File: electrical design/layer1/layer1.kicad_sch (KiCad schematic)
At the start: 95 parts, among them J1 Conn_01x08_Male, J2 Conn_01x06_Female, SW1 SW_DPDT_x2, SW2 SW_DPDT_x2, SW3 SW_Push, U1 STM32F103C8T6, U2 CD74HC4067SM, U3 CD74HC4067SM, Y1 8MHz

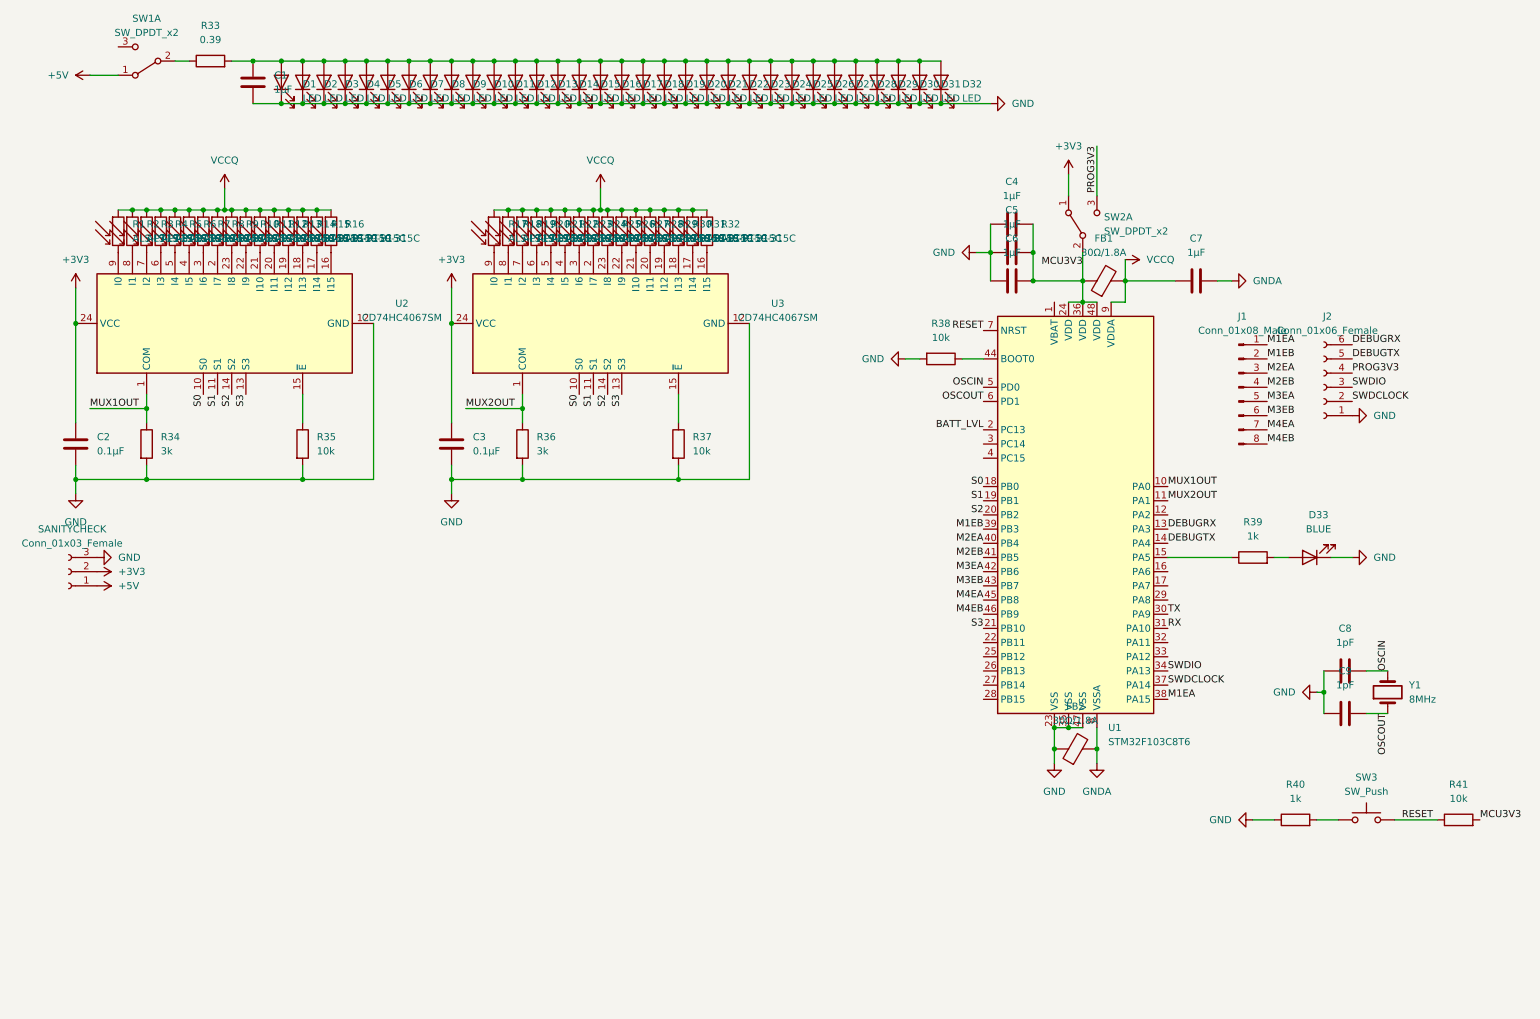
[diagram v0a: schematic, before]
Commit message: add solenoid circuit and custom board rules
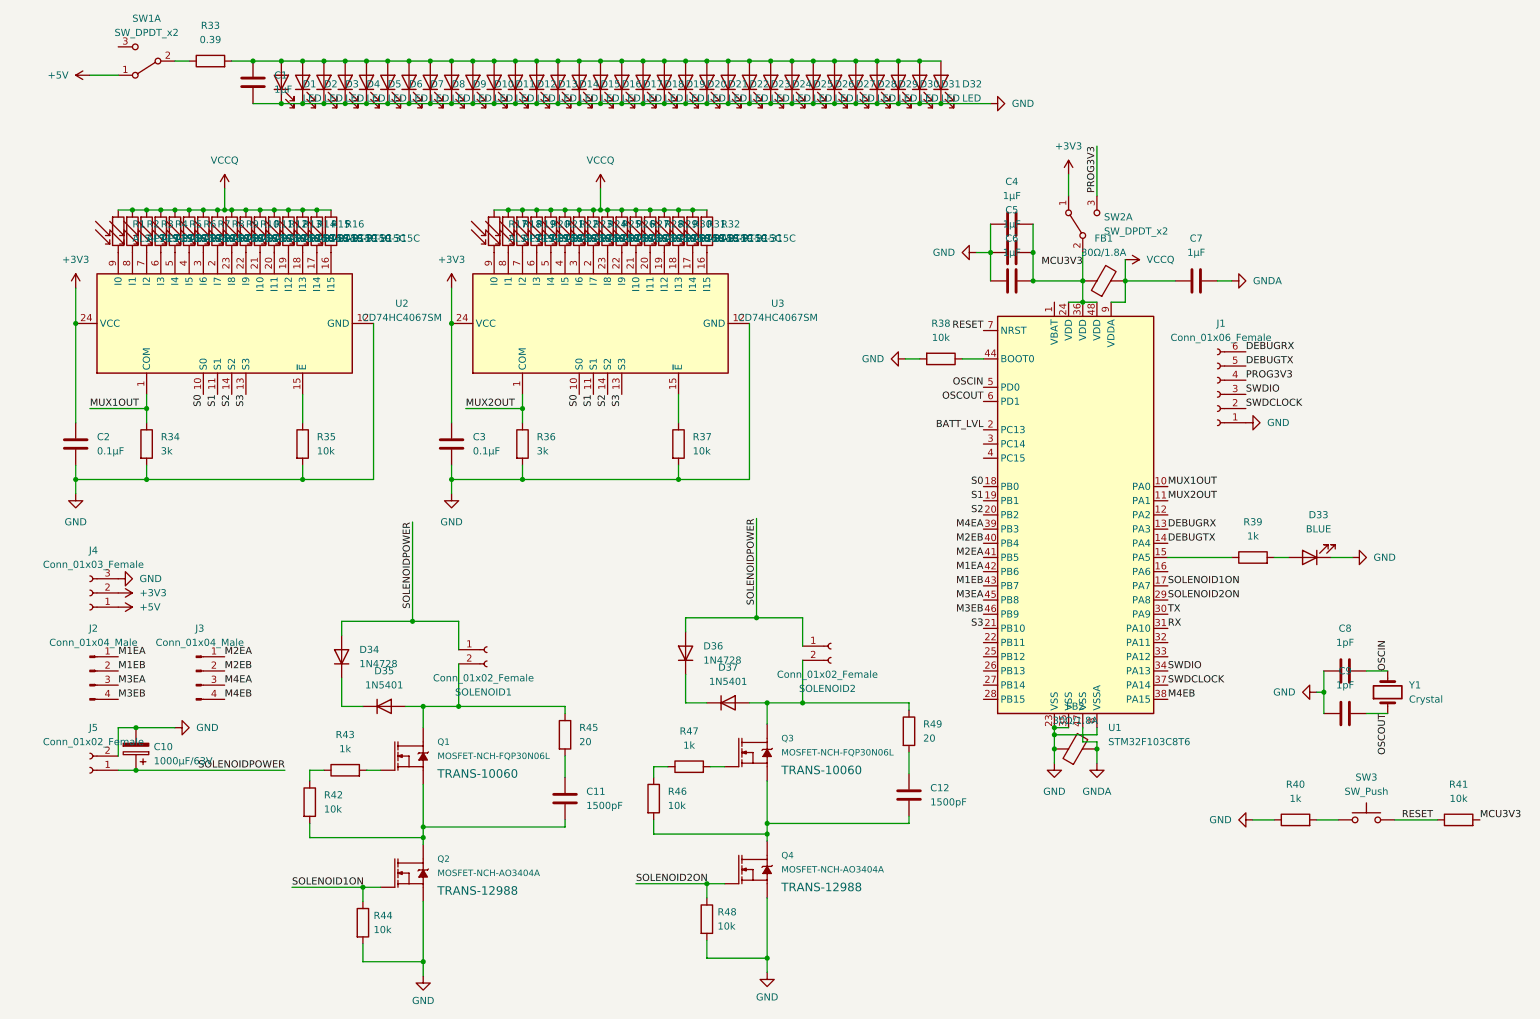
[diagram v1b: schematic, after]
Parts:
- removed J1: Conn_01x08_Male, symbol Connector:Conn_01x08_Male
- added C10: 1000µF/63V, Capacitor_THT:CP_Radial_D16.0mm_P7.50mm, symbol Device:C_Polarized
- added C11, C12: 1500pF, Capacitor_SMD:C_0603_1608Metric, symbol Device:C
- added D34, D36: 1N4728, Diode_THT:D_DO-41_SOD81_P10.16mm_Horizontal, symbol Device:D
- added D35, D37: 1N5401, Diode_THT:D_DO-27_P15.24mm_Horizontal, symbol Device:D
- added J2, J3: Conn_01x04_Male, Connector_PinHeader_2.54mm:PinHeader_1x04_P2.54mm_Vertical, symbol Connector:Conn_01x04_Male
- added J5, SOLENOID1, SOLENOID2: Conn_01x02_Female, Connector_AMASS:AMASS_XT30UPB-F_1x02_P5.0mm_Vertical, symbol Connector:Conn_01x02_Female
- added Q1, Q3: MOSFET-NCH-FQP30N06L, Package_TO_SOT_THT:TO-220-3_Vertical, symbol SparkFun-DiscreteSemi:MOSFET-NCH-FQP30N06L
- added Q2, Q4: MOSFET-NCH-AO3404A, Package_TO_SOT_SMD:TSOT-23, symbol SparkFun-DiscreteSemi:MOSFET-NCH-AO3404A
- added R42, R44, R46, R48: 10k, Resistor_SMD:R_0603_1608Metric, symbol Device:R
- added R43, R47: 1k, Resistor_SMD:R_0603_1608Metric, symbol Device:R
- added R45, R49: 20, Resistor_SMD:R_0603_1608Metric, symbol Device:R
- C2, C3, C4, C5, C6, C7, FB1, FB2: footprint (none) -> Capacitor_SMD:C_0603_1608Metric
- C8, C9: footprint Capacitors:0603 -> Capacitor_SMD:C_0603_1608Metric
- D33: footprint (none) -> Diode_SMD:D_0603_1608Metric
- J4: renamed from SANITYCHECK; footprint (none) -> Connector_PinHeader_2.54mm:PinHeader_1x03_P2.54mm_Vertical
- R1, R10, R11, R12, R13, R14, R15, R16, R17, R18, R19, R2, R20, R21, R22, R23, R24, R25, R26, R27, R28, R29, R3, R30, R31, R32, R4, R5, R6, R7, R8, R9: footprint Diode_SMD:D_0201_0603Metric -> Resistor_SMD:R_0603_1608Metric
- R33, R34, R35, R36, R37, R38, R39, R40, R41: footprint (none) -> Resistor_SMD:R_0603_1608Metric
- SW3: footprint (none) -> Button_Switch_SMD:SW_Push_SPST_NO_Alps_SKRK
- Y1: value 8MHz -> Crystal
- renumbered J2 to J1
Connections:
- net GND: now also U1.8 (VSSA), C10.2, J5.2 (Pin_2), Q2.2 (S), Q4.2 (S), R44.2, R48.2; no longer U1.47 (VSS)
- net GNDA: now also U1.47 (VSS); no longer U1.8 (VSSA)
- net M1EA: now also U1.42 (PB6), J2.1 (Pin_1); no longer U1.38 (PA15)
- net M1EB: now also U1.43 (PB7), J2.2 (Pin_2); no longer U1.39 (PB3)
- net M2EA: now also U1.41 (PB5), J3.1 (Pin_1); no longer U1.40 (PB4)
- net M2EB: now also U1.40 (PB4), J3.2 (Pin_2); no longer U1.41 (PB5)
- net M3EA: now also U1.45 (PB8), J2.3 (Pin_3); no longer U1.42 (PB6)
- net M3EB: now also U1.46 (PB9), J2.4 (Pin_4); no longer U1.43 (PB7)
- net M4EA: now also U1.39 (PB3), J3.3 (Pin_3); no longer U1.45 (PB8)
- net M4EB: now also U1.38 (PA15), J3.4 (Pin_4); no longer U1.46 (PB9)
- net SOLENOID1ON: now reaches U1.17 (PA7)
- net SOLENOID1ON: now also Q2.1 (G), R44.1
- net SOLENOID2ON: now reaches U1.29 (PA8)
- net SOLENOID2ON: now also Q4.1 (G), R48.1
- new net: R42.1, R43.1
- new net: Q1.1 (G), R43.2
- new net: Q3.1 (G), R47.2
- new net: D37.2 (A), Q3.2 (D), R49.1, SOLENOID2.2 (Pin_2)
- new net: C12.2, Q3.3 (S), Q4.3 (D), R46.2
- new net: C11.2, Q1.3 (S), Q2.3 (D), R42.2
- new net: D36.1 (K), D37.1 (K)
- new net: D35.2 (A), Q1.2 (D), R45.1, SOLENOID1.2 (Pin_2)
- new net: R46.1, R47.1
- new net: C12.1, R49.2
- new net: D34.1 (K), D35.1 (K)
- new net: C11.1, R45.2
- new net SOLENOIDPOWER: C10.1, D34.2 (A), D36.2 (A), J5.1 (Pin_1), SOLENOID1.1 (Pin_1), SOLENOID2.1 (Pin_1)
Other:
- moved on the sheet: J1, J4

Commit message: update layer 1 and layer 3 pcbs
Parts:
- removed C12: 1500pF, Capacitor_SMD:C_0603_1608Metric, symbol Device:C
- removed D36: 1N4728, Diode_THT:D_DO-41_SOD81_P10.16mm_Horizontal, symbol Device:D
- removed D37: 1N5401, Diode_THT:D_DO-27_P15.24mm_Horizontal, symbol Device:D
- removed J2, J3: Conn_01x04_Male, Connector_PinHeader_2.54mm:PinHeader_1x04_P2.54mm_Vertical, symbol Connector:Conn_01x04_Male
- removed Q3: MOSFET-NCH-FQP30N06L, Package_TO_SOT_THT:TO-220-3_Vertical, symbol SparkFun-DiscreteSemi:MOSFET-NCH-FQP30N06L
- removed Q4: MOSFET-NCH-AO3404A, Package_TO_SOT_SMD:TSOT-23, symbol SparkFun-DiscreteSemi:MOSFET-NCH-AO3404A
- removed R46, R48: 10k, Resistor_SMD:R_0603_1608Metric, symbol Device:R
- removed R47: 1k, Resistor_SMD:R_0603_1608Metric, symbol Device:R
- removed R49: 20, Resistor_SMD:R_0603_1608Metric, symbol Device:R
- removed SOLENOID2: Conn_01x02_Female, Connector_AMASS:AMASS_XT30UPB-F_1x02_P5.0mm_Vertical, symbol Connector:Conn_01x02_Female
- J1: value Conn_01x06_Female -> SH1.0 Female
- SW1, SW2: footprint (none) -> Switches:SWITCH_SPDT_PTH_11.6X4.0MM_LOCK
- Y1: footprint Clocks:CRYSTAL-SMD-5X3.2-2PAD -> Crystal:Crystal_SMD_5032-2Pin_5.0x3.2mm
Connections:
- net M1EA: no longer names the net of U1.42 (PB6)
- net M1EB: no longer names the net of U1.43 (PB7)
- net M2EA: no longer names the net of U1.41 (PB5)
- net M2EB: no longer names the net of U1.40 (PB4)
- net M3EA: no longer names the net of U1.45 (PB8)
- net M3EB: no longer names the net of U1.46 (PB9)
- net M4EA: no longer names the net of U1.39 (PB3)
- net M4EB: no longer names the net of U1.38 (PA15)
- net SOLENOID1ON renamed SOLENOIDON
- net SOLENOID2ON: no longer names the net of U1.29 (PA8)

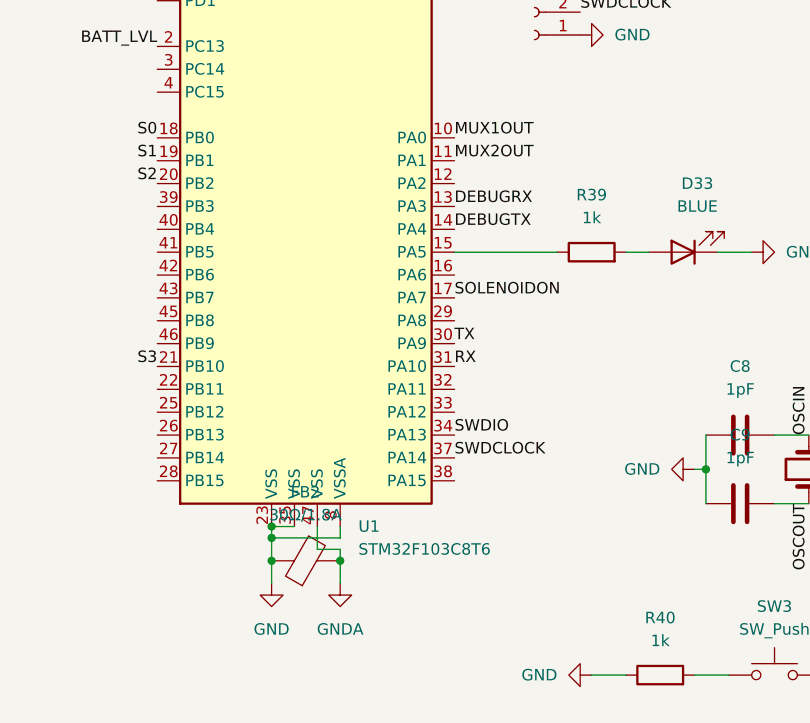
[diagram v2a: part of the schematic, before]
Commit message: update l1, l3, and driver pcbs
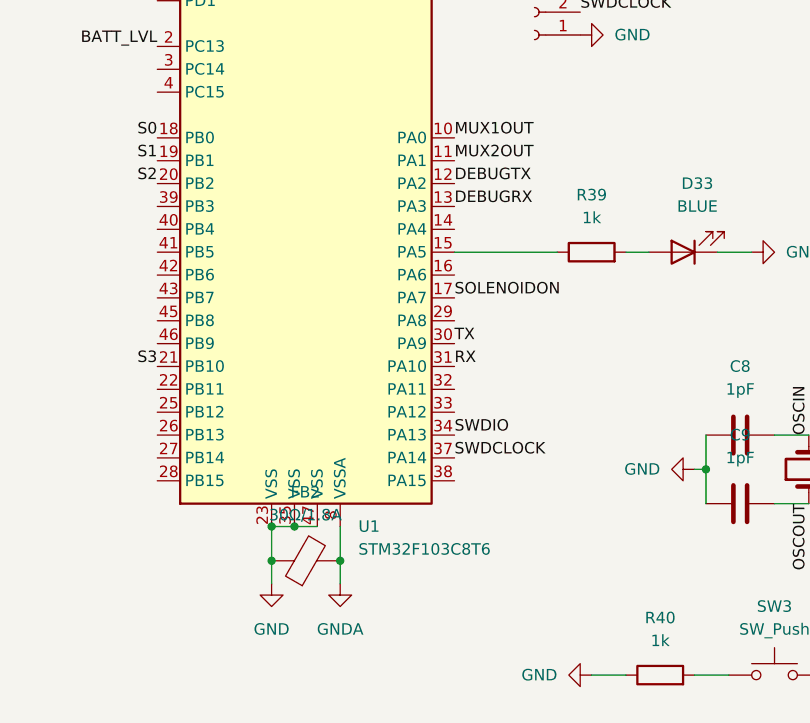
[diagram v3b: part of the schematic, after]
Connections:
- net DEBUGTX: now also U1.12 (PA2); no longer U1.14 (PA4)
- net GND: now also U1.47 (VSS); no longer U1.8 (VSSA)
- net GNDA: now also U1.8 (VSSA); no longer U1.47 (VSS)
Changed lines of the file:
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@@
   (junction (at 58.42 25.4) (diameter 0) (color 0 0 0 0)
   )
-  (junction (at 196.85 146.05) (diameter 0) (color 0 0 0 0)
-  )
   (junction (at 123.19 25.4) (diameter 0) (color 0 0 0 0)
   )
@@
   (junction (at 115.57 52.07) (diameter 0) (color 0 0 0 0)
   )
+  (junction (at 199.39 144.78) (diameter 0) (color 0 0 0 0)
+  )
   (junction (at 66.04 33.02) (diameter 0) (color 0 0 0 0)
   )
@@
     (stroke (width 0) (type default) (color 0 0 0 0))
   )
-  (wire (pts (xy 196.85 144.78) (xy 196.85 146.05))
-    (stroke (width 0) (type default) (color 0 0 0 0))
-  )
   (wire (pts (xy 52.07 52.07) (xy 54.61 52.07))
     (stroke (width 0) (type default) (color 0 0 0 0))
@@
     (stroke (width 0) (type default) (color 0 0 0 0))
   )
-  (wire (pts (xy 196.85 146.05) (xy 196.85 148.59))
+  (wire (pts (xy 196.85 144.78) (xy 196.85 148.59))
     (stroke (width 0) (type default) (color 0 0 0 0))
   )
@@
     (stroke (width 0) (type default) (color 0 0 0 0))
   )
-  (wire (pts (xy 204.47 147.32) (xy 204.47 148.59))
-    (stroke (width 0) (type default) (color 0 0 0 0))
-  )
   (wire (pts (xy 199.39 68.58) (xy 201.93 68.58))
     (stroke (width 0) (type default) (color 0 0 0 0))
@@
     (stroke (width 0) (type default) (color 0 0 0 0))
   )
-  (wire (pts (xy 204.47 144.78) (xy 204.47 146.05))
-    (stroke (width 0) (type default) (color 0 0 0 0))
-  )
   (wire (pts (xy 54.61 52.07) (xy 57.15 52.07))
     (stroke (width 0) (type default) (color 0 0 0 0))
@@
     (stroke (width 0) (type default) (color 0 0 0 0))
   )
-  (wire (pts (xy 201.93 144.78) (xy 201.93 147.32))
-    (stroke (width 0) (type default) (color 0 0 0 0))
-  )
   (wire (pts (xy 53.34 25.4) (xy 58.42 25.4))
     (stroke (width 0) (type default) (color 0 0 0 0))
@@
     (stroke (width 0) (type default) (color 0 0 0 0))
   )
+  (wire (pts (xy 204.47 144.78) (xy 204.47 148.59))
+    (stroke (width 0) (type default) (color 0 0 0 0))
+  )
   (wire (pts (xy 96.52 33.02) (xy 100.33 33.02))
     (stroke (width 0) (type default) (color 0 0 0 0))
@@
     (stroke (width 0) (type default) (color 0 0 0 0))
   )
-  (wire (pts (xy 201.93 147.32) (xy 204.47 147.32))
-    (stroke (width 0) (type default) (color 0 0 0 0))
-  )
   (wire (pts (xy 58.42 25.4) (xy 62.23 25.4))
     (stroke (width 0) (type default) (color 0 0 0 0))
@@
     (stroke (width 0) (type default) (color 0 0 0 0))
   )
+  (wire (pts (xy 199.39 144.78) (xy 201.93 144.78))
+    (stroke (width 0) (type default) (color 0 0 0 0))
+  )
   (wire (pts (xy 204.47 148.59) (xy 204.47 151.13))
     (stroke (width 0) (type default) (color 0 0 0 0))
@@
     (stroke (width 0) (type default) (color 0 0 0 0))
   )
-  (wire (pts (xy 204.47 146.05) (xy 196.85 146.05))
-    (stroke (width 0) (type default) (color 0 0 0 0))
-  )
   (wire (pts (xy 62.23 100.33) (xy 34.29 100.33))
     (stroke (width 0) (type default) (color 0 0 0 0))
@@
     (effects (font (size 1.27 1.27)) (justify right bottom))
   )
+  (label "DEBUGTX" (at 217.17 106.68 0)
+    (effects (font (size 1.27 1.27)) (justify left bottom))
+  )
   (label "PROG3V3" (at 204.47 40.64 270)
     (effects (font (size 1.27 1.27)) (justify right bottom))
@@
     (effects (font (size 1.27 1.27)) (justify right bottom))
   )
-  (label "DEBUGTX" (at 217.17 111.76 0)
-    (effects (font (size 1.27 1.27)) (justify left bottom))
-  )
   (label "OSCOUT" (at 184.15 86.36 180)

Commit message: almost final pcbs
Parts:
- added J2: SH1.0 5P, Connector_JST:JST_SH_BM05B-SRSS-TB_1x05-1MP_P1.00mm_Vertical, symbol Connector:Conn_01x05_Male
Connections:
- net +3V3: now also J2.4 (Pin_4)
- net +5V: now also J2.3 (Pin_3)
- net GND: now also J2.5 (Pin_5)
- net RX: now also J2.1 (Pin_1)
- net TX: now also J2.2 (Pin_2)
- net BATT_LVL: no longer names the net of U1.2 (PC13)
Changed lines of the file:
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@@
   (title_block
     (title "layer 1 schematic drawing")
-    (date "2023-01-10")
-    (rev "v0.4")
+    (date "2023-02-05")
+    (rev "v0.5")
     (company "8076 Robotics")
   )
@@
     (effects (font (size 1.27 1.27)) (justify right bottom))
   )
+  (label "RX" (at 146.05 173.99 0)
+    (effects (font (size 1.27 1.27)) (justify left bottom))
+  )
   (label "RX" (at 217.17 127 0)
     (effects (font (size 1.27 1.27)) (justify left bottom))
@@
     (effects (font (size 1.27 1.27)) (justify left bottom))
   )
+  (label "TX" (at 146.05 176.53 0)
+    (effects (font (size 1.27 1.27)) (justify left bottom))
+  )
   (label "S3" (at 119.38 85.09 270)
     (effects (font (size 1.27 1.27)) (justify right bottom))
@@
     (effects (font (size 1.27 1.27)) (justify left bottom))
   )
-  (label "BATT_LVL" (at 184.15 91.44 180)
-    (effects (font (size 1.27 1.27)) (justify right bottom))
-  )
   (label "S0" (at 44.45 85.09 270)
     (effects (font (size 1.27 1.27)) (justify right bottom))
@@
     (pin "2")
   )
+  (symbol (lib_id "power:+3V3") (at 146.05 181.61 270) (unit 1)
+    (in_bom yes) (on_board yes) (fields_autoplaced)
+    (property "Reference" "#PWR022" (id 0) (at 142.24 181.61 0)
+      (effects (font (size 1.27 1.27)) hide)
+    )
+    (property "Value" "+3V3" (id 1) (at 149.86 181.6099 90)
+      (effects (font (size 1.27 1.27)) (justify left))
+    )
+    (property "Footprint" "" (id 2) (at 146.05 181.61 0)
+      (effects (font (size 1.27 1.27)) hide)
+    )
+    (property "Datasheet" "" (id 3) (at 146.05 181.61 0)
+      (effects (font (size 1.27 1.27)) hide)
+    )
+    (pin "1")
+  )
   (symbol (lib_id "power:VCCQ") (at 209.55 60.96 270) (unit 1)
     (in_bom yes) (on_board yes) (fields_autoplaced)
@@
     (pin "2")
   )
+  (symbol (lib_id "Connector:Conn_01x05_Male") (at 140.97 179.07 0) (unit 1)
+    (in_bom yes) (on_board yes) (fields_autoplaced)
+    (property "Reference" "J2" (id 0) (at 141.605 168.91 0))
+    (property "Value" "SH1.0 5P" (id 1) (at 141.605 171.45 0))
+    (property "Footprint" "Connector_JST:JST_SH_BM05B-SRSS-TB_1x05-1MP_P1.00mm_Vertical" (id 2) (at 140.97 179.07 0)
+      (effects (font (size 1.27 1.27)) hide)
+    )
+    (property "Datasheet" "~" (id 3) (at 140.97 179.07 0)
+      (effects (font (size 1.27 1.27)) hide)
+    )
+    (pin "1")
+    (pin "2")
+    (pin "3")
+    (pin "4")
+    (pin "5")
+  )
   (symbol (lib_id "Connector:Conn_01x02_Female") (at 24.13 152.4 180) (unit 1)
     (in_bom yes) (on_board yes) (fields_autoplaced)
@@
     (pin "1")
   )
+  (symbol (lib_id "power:+5V") (at 146.05 179.07 270) (unit 1)
+    (in_bom yes) (on_board yes) (fields_autoplaced)
+    (property "Reference" "#PWR021" (id 0) (at 142.24 179.07 0)
+      (effects (font (size 1.27 1.27)) hide)
+    )
+    (property "Value" "+5V" (id 1) (at 149.86 179.0699 90)
+      (effects (font (size 1.27 1.27)) (justify left))
+    )
+    (property "Footprint" "" (id 2) (at 146.05 179.07 0)
+      (effects (font (size 1.27 1.27)) hide)
+    )
+    (property "Datasheet" "" (id 3) (at 146.05 179.07 0)
+      (effects (font (size 1.27 1.27)) hide)
+    )
+    (pin "1")
+  )
   (symbol (lib_id "Device:R") (at 101.6 93.98 0) (unit 1)
     (in_bom yes) (on_board yes) (fields_autoplaced)
@@
     (pin "2")
   )
+  (symbol (lib_id "power:GND") (at 146.05 184.15 90) (unit 1)
+    (in_bom yes) (on_board yes) (fields_autoplaced)
+    (property "Reference" "#PWR023" (id 0) (at 152.4 184.15 0)
+      (effects (font (size 1.27 1.27)) hide)
+    )
+    (property "Value" "GND" (id 1) (at 149.86 184.1499 90)
+      (effects (font (size 1.27 1.27)) (justify right))
+    )
+    (property "Footprint" "" (id 2) (at 146.05 184.15 0)
+      (effects (font (size 1.27 1.27)) hide)
+    )
+    (property "Datasheet" "" (id 3) (at 146.05 184.15 0)
+      (effects (font (size 1.27 1.27)) hide)
+    )
+    (pin "1")
+  )
   (symbol (lib_id "MCU_ST_STM32F1:STM32F103C8Tx") (at 201.93 106.68 0) (unit 1)
     (in_bom yes) (on_board yes) (fields_autoplaced)
@@
       (reference "#PWR020") (unit 1) (value "GND") (footprint "")
     )
+    (path "/a24a6bcb-05a3-48db-a974-3af54d2022be"
+      (reference "#PWR021") (unit 1) (value "+5V") (footprint "")
+    )
+    (path "/302a046c-85ff-41f3-888d-f2cbfe51ba1d"
+      (reference "#PWR022") (unit 1) (value "+3V3") (footprint "")
+    )
+    (path "/b363095e-1ed9-418d-b12d-de3911db4f36"
+      (reference "#PWR023") (unit 1) (value "GND") (footprint "")
+    )
     (path "/2aea5601-d7e4-47c3-b7da-c0e856d55909"
       (reference "#PWR0101") (unit 1) (value "+5V") (footprint "")
@@
       (reference "J1") (unit 1) (value "SH1.0 Female") (footprint "Connector_JST:JST_SH_BM06B-SRSS-TB_1x06-1MP_P1.00mm_Vertical")
     )
+    (path "/6f4d7466-bc05-4cd6-8b0c-175c4fdb3fde"
+      (reference "J2") (unit 1) (value "SH1.0 5P") (footprint "Connector_JST:JST_SH_BM05B-SRSS-TB_1x05-1MP_P1.00mm_Vertical")
+    )
     (path "/86937535-1a00-4375-a966-feffacfd480e"
